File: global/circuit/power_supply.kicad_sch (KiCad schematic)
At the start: 12 parts, among them U1 LMR62014XMF-NOPB, U5 TLV767

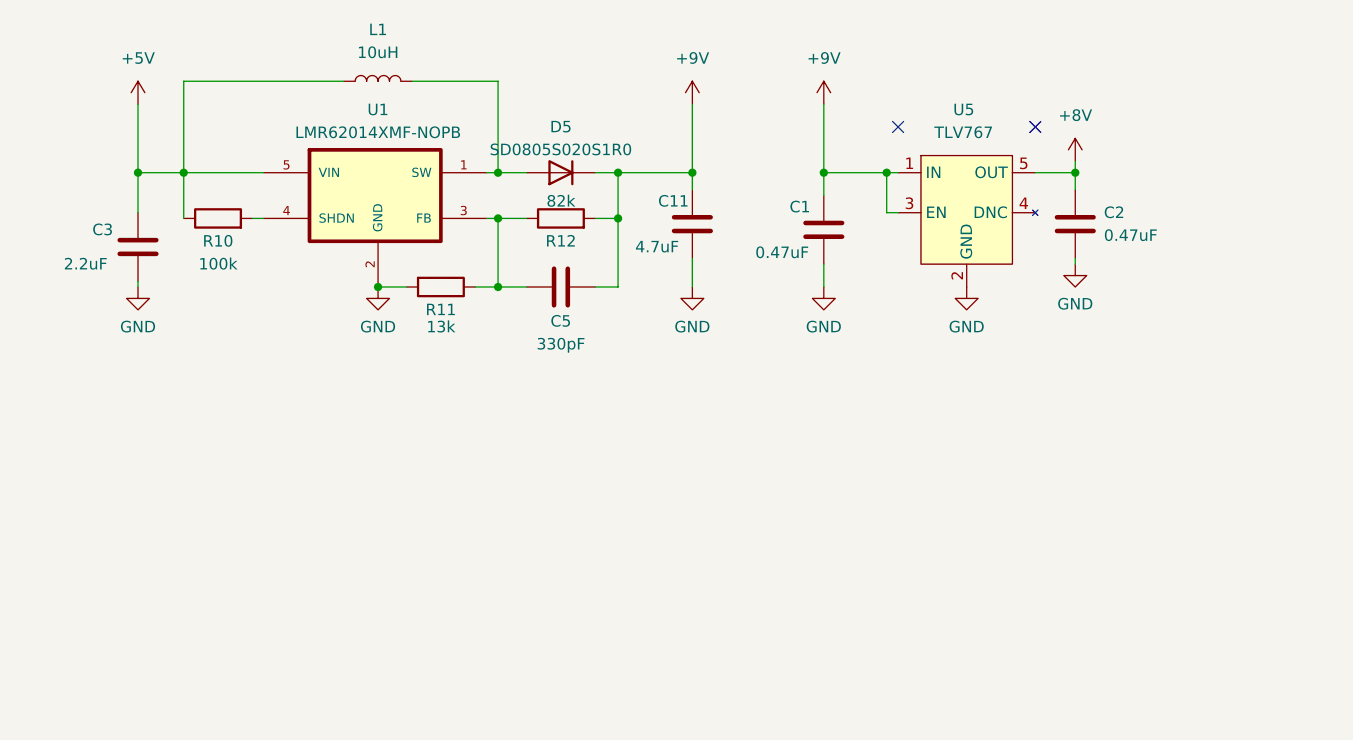
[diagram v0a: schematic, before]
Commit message: rework distortion circuit and simulations
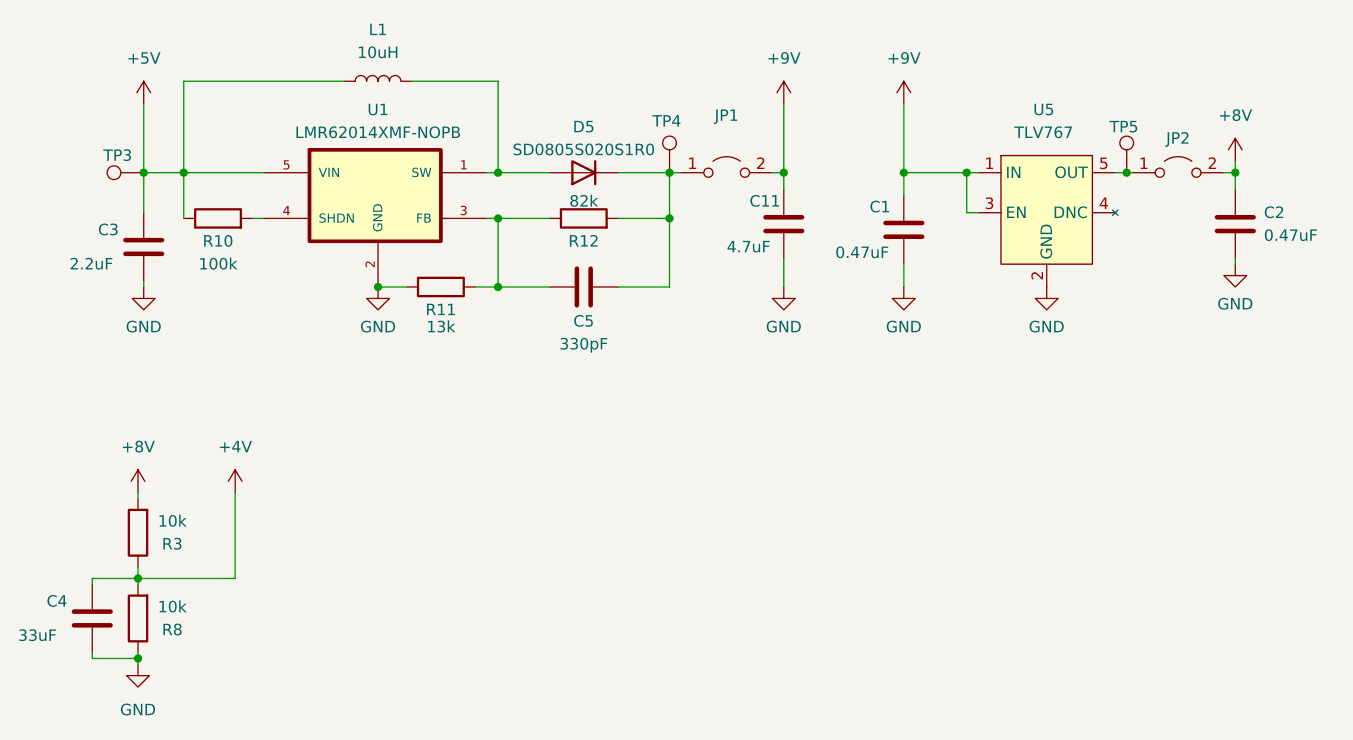
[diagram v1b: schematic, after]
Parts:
- added C4: 33uF, Capacitor_SMD:C_1206_3216Metric_Pad1.33x1.80mm_HandSolder, symbol Device:C
- added JP1, JP2: Jumper_2_Open, Resistor_SMD:R_0805_2012Metric_Pad1.20x1.40mm_HandSolder, symbol Jumper:Jumper_2_Open
- added R3, R8: 10k, Resistor_SMD:R_0805_2012Metric_Pad1.20x1.40mm_HandSolder, symbol Device:R
- added TP3, TP4, TP5: TestPoint, TestPoint:TestPoint_THTPad_1.0x1.0mm_Drill0.5mm, symbol Connector:TestPoint
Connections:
- net +5V: now also TP3.1
- net +8V: now also JP2.2 (B), R3.2; no longer U5.5 (OUT)
- net +9V: now also JP1.2 (B); no longer C5.2, D5.1 (K), R12.2
- net GND: now also C4.2, R8.1
- new net: C5.2, D5.1 (K), JP1.1 (A), R12.2, TP4.1
- new net: JP2.1 (A), TP5.1, U5.5 (OUT)
- new net +4V: C4.1, R3.1, R8.2
- no-connect marks 2 -> 0
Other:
- moved on the sheet: C1, C11, C2, C3, C5, D5, R12, U5

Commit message: rework global circuits
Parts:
- L?: renamed from L1; footprint Inductor_SMD:L_Abracon_ASPI-3012S -> Inductor_SMD:L_0805_2012Metric_Pad1.15x1.40mm_HandSolder
- renumbered C2 to C?, C5 to C?, C4 to C?, C3 to C?, C11 to C?, C1 to C?, D5 to D?, JP1 to JP?, JP2 to JP?, R3 to R?, R10 to R?, R11 to R?, R12 to R?, R8 to R?, TP3 to TP?, TP5 to TP?, TP4 to TP?, U5 to U?, U1 to U?

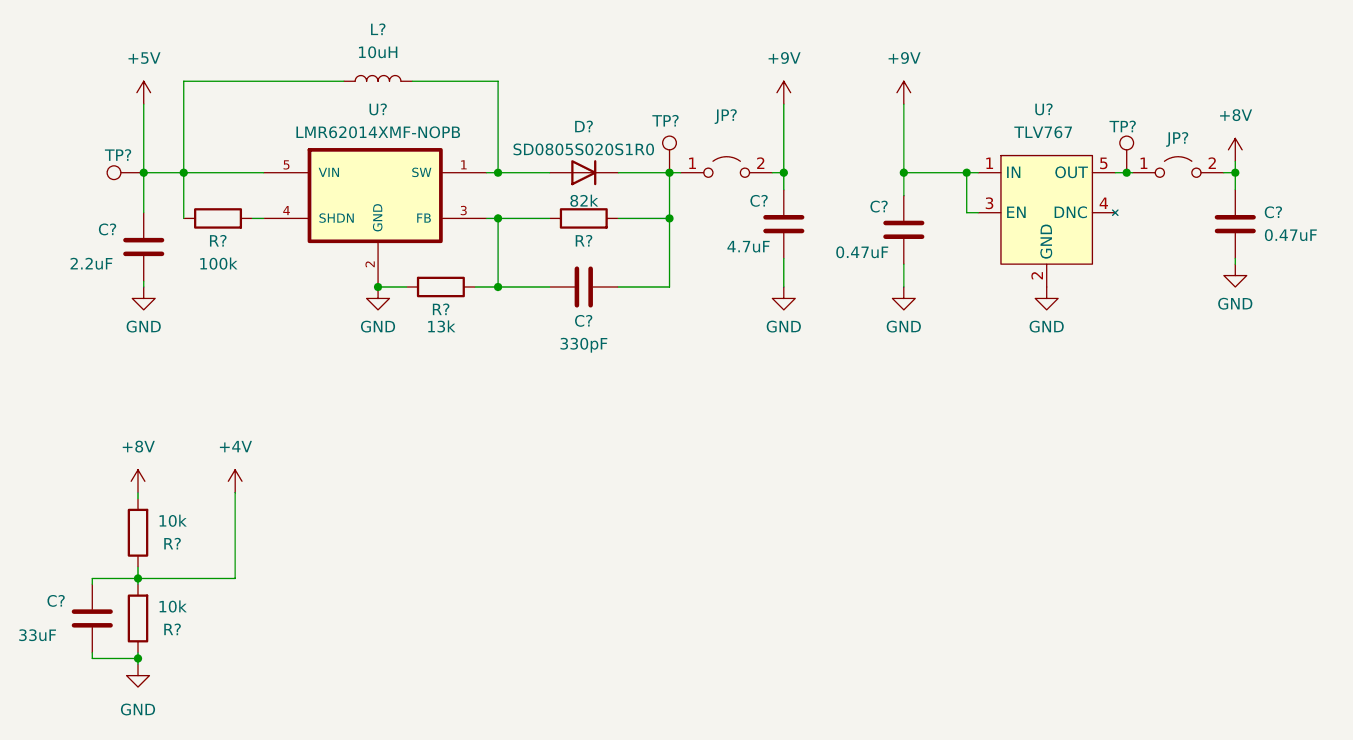
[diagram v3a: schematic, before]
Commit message: minor circuit rework for better use with multiple projects
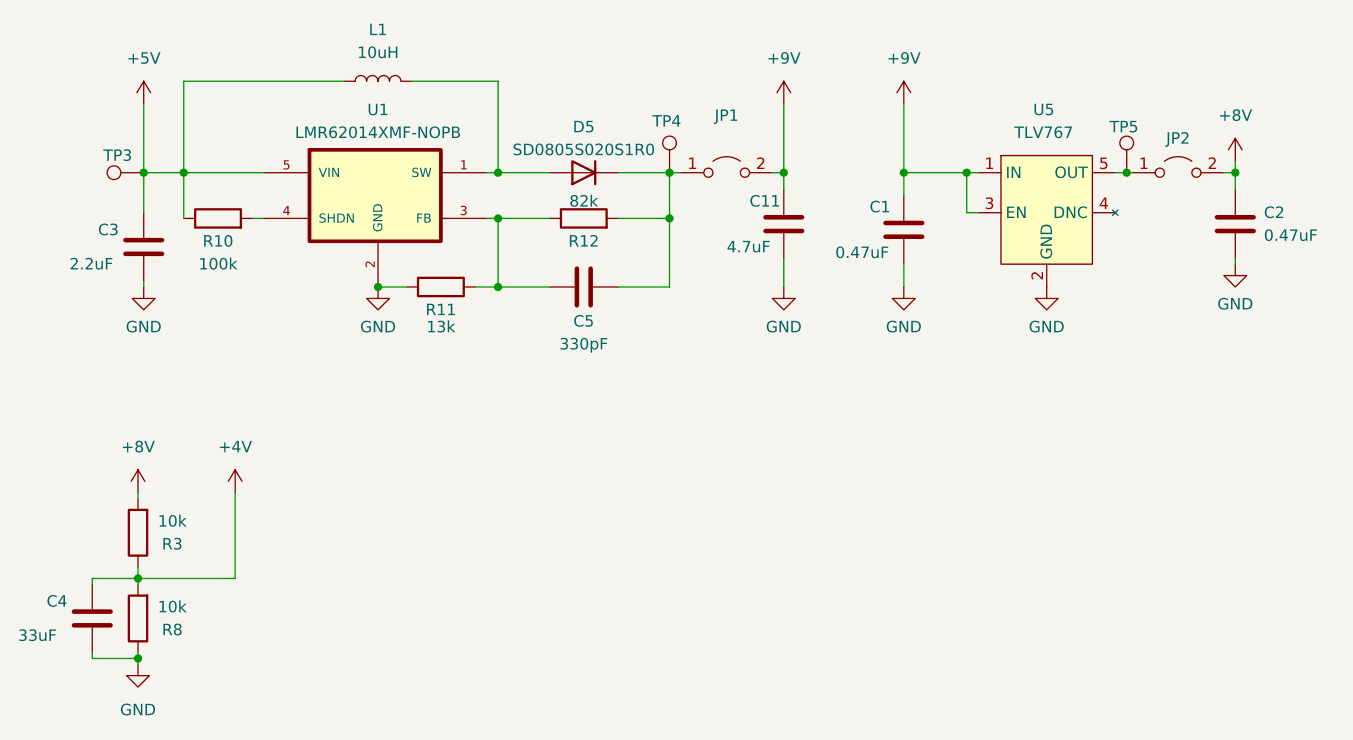
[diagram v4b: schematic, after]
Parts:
- L1: renamed from L?; footprint Inductor_SMD:L_0805_2012Metric_Pad1.15x1.40mm_HandSolder -> Inductor_SMD:L_Abracon_ASPI-3012S
- gave numbers to parts that had none: 19
